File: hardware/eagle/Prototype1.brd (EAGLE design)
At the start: 100 x 80 mm, 27 parts, among them U1 ARDUINO_SHIELDLABEL

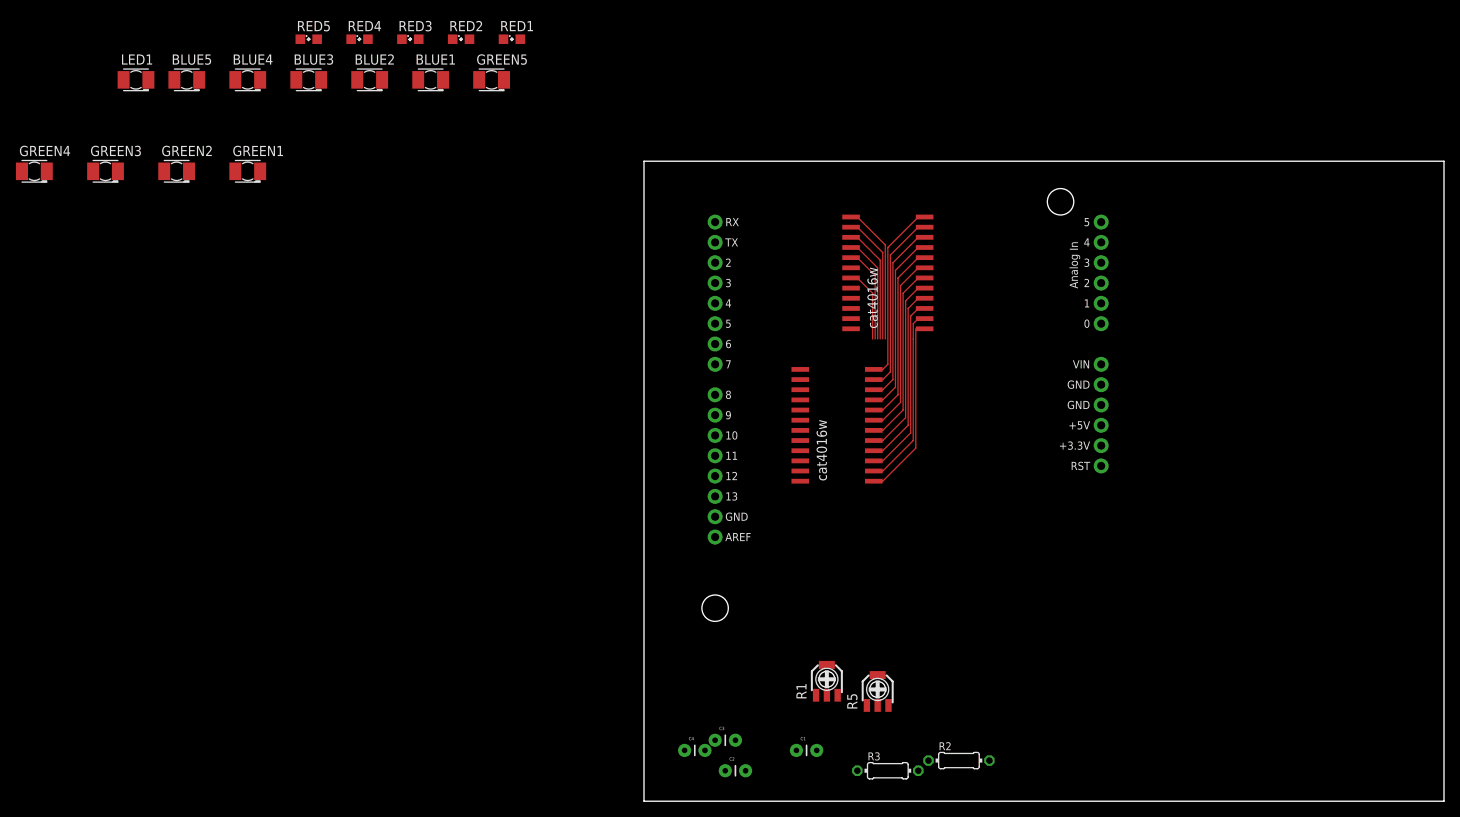
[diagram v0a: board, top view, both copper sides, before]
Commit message: cat4016 hat nun kleine Füsse
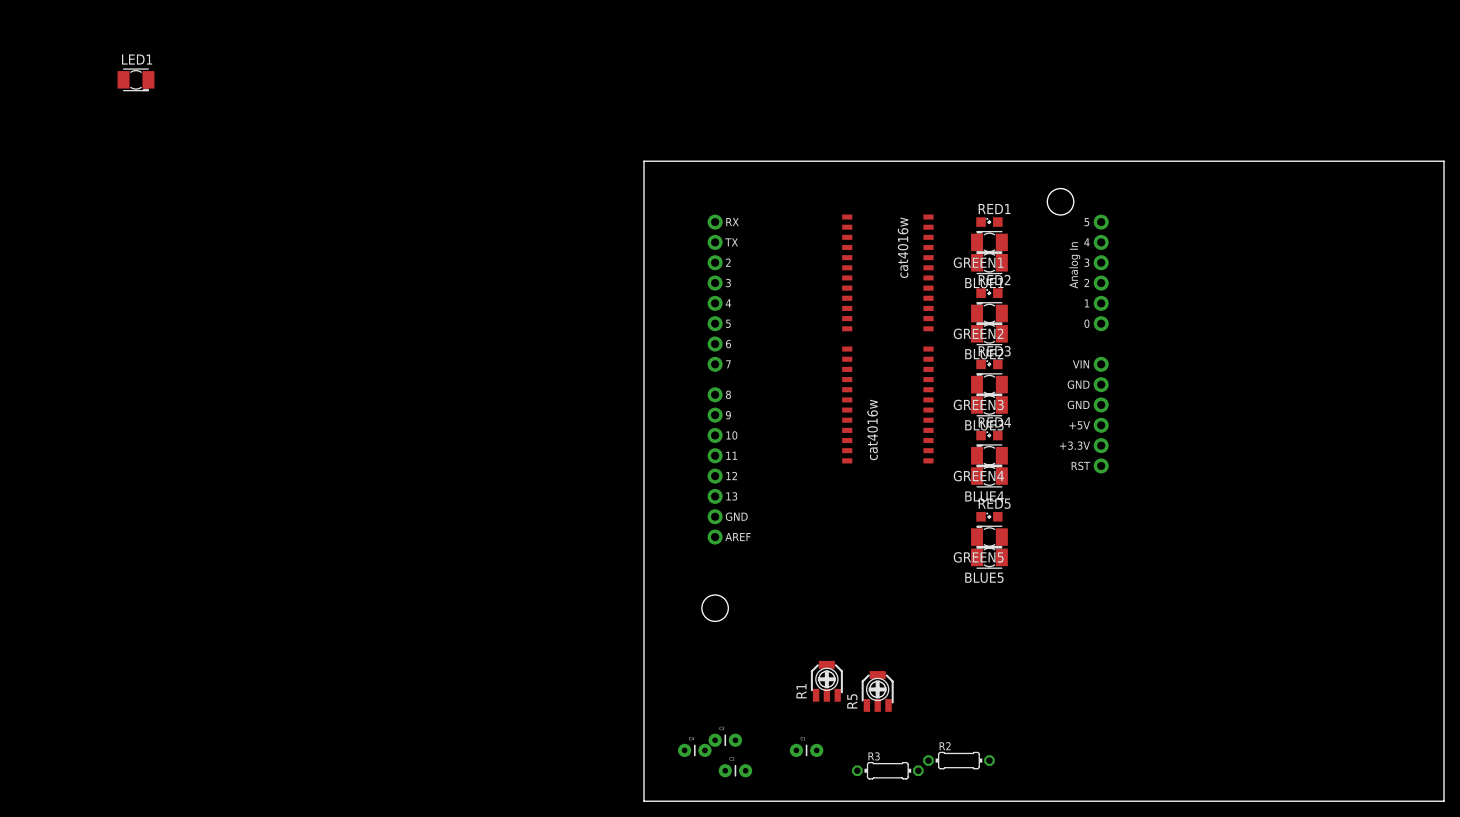
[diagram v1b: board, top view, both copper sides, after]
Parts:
- moved GREEN4 124.6 mm to (43.2, 43.2), turned to 180 degrees
- moved BLUE5 116.7 mm to (43.2, 30.5), turned to 180 degrees
- moved GREEN3 113.7 mm to (43.2, 52.1), turned to 180 degrees
- moved BLUE4 105.1 mm to (43.2, 40.6), turned to 180 degrees
- moved RED5 103.9 mm to (43.2, 35.6)
- moved GREEN2 103.1 mm to (43.2, 61.0), turned to 180 degrees
- moved BLUE3 94.3 mm to (43.2, 49.5), turned to 180 degrees
- moved GREEN1 93.1 mm to (43.2, 69.8), turned to 180 degrees
- moved RED4 93.0 mm to (43.2, 45.7)
- moved GREEN5 84.5 mm to (43.2, 33.0), turned to 180 degrees
- moved BLUE2 83.7 mm to (43.2, 58.4), turned to 180 degrees
- moved RED3 83.0 mm to (43.2, 54.6)
- moved BLUE1 73.5 mm to (43.2, 67.3), turned to 180 degrees
- moved RED2 73.3 mm to (43.2, 63.5)
- moved RED1 63.9 mm to (43.2, 72.4)
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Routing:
- net N$21: track 22.8 -> 0.00 mm
- net N$8: track 22.8 -> 0.00 mm
- net N$25: track 22.8 -> 0.00 mm
- net N$24: track 22.8 -> 0.00 mm
- net N$7: track 22.8 -> 0.00 mm
- net N$23: track 22.8 -> 0.00 mm
- net N$19: track 22.8 -> 0.00 mm
- net N$22: track 22.8 -> 0.00 mm
- net N$20: track 22.8 -> 0.00 mm
- net N$18: track 22.0 -> 0.00 mm
- net GND: track 21.9 -> 0.00 mm
- net N$9: track 19.2 -> 0.00 mm
- net N$17: track 17.5 -> 0.00 mm
- net N$15: track 16.1 -> 0.00 mm
- net N$16: track 14.7 -> 0.00 mm
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
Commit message: Wege bahnen WIP
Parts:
- removed LED1: (no value), led:KA-3528ASYC
- moved C2 64.1 mm to (31.8, 64.1)
- moved C1 61.0 mm to (31.8, 66.0)
- moved C4 26.2 mm to (21.6, 26.7)
- moved C3 24.5 mm to (21.6, 28.6)
- moved R2 23.7 mm to (33.0, 27.9), turned to 180 degrees
- moved R1 14.6 mm to (8.26, 15.2)
- moved R3 13.3 mm to (17.8, 7.62)
- moved U$2 12.1 mm to (29.2, 54.0)
- moved U$3 12.1 mm to (29.2, 37.5)
- moved R5 11.0 mm to (31.1, 24.8), turned to 270 degrees
- moved RED1 4.62 mm to (44.5, 67.9)
- moved GREEN5 4.62 mm to (44.5, 28.6)
- moved RED5 4.62 mm to (44.5, 31.1)
- moved BLUE1 4.62 mm to (44.5, 62.9)
- moved BLUE2 4.62 mm to (44.5, 54.0)
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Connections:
- net N$11: now also RED5.C, U$2.6; no longer BLUE5.C, U$2.19
- net N$12: now also U$2.7; no longer U$2.18
- net N$13: now also BLUE5.C, U$2.8; no longer RED5.C, U$2.17
- net N$14: now also U$2.9; no longer U$2.16
- net N$15: now also U$2.11; no longer U$2.14
- net N$16: now also U$2.10; no longer U$2.15
- net N$17: now also U$2.12; no longer U$2.13
- net N$18: now also U$2.13; no longer U$2.12
- net N$19: now also U$2.14; no longer U$2.11
- net N$20: now also U$2.15; no longer U$2.10
- net N$21: now also U$2.16; no longer U$2.9
- net N$22: now also U$2.17; no longer U$2.8
- net N$23: now also U$2.18; no longer U$2.7
- net N$24: now also U$2.19; no longer U$2.6
- net N$25: now also U$2.20; no longer U$2.5
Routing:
- net +5V: track 0.00 -> 163.7 mm
- net N$25: track 0.00 -> 42.4 mm
- net N$24: track 0.00 -> 37.5 mm
- net N$23: track 0.00 -> 32.6 mm
- net N$8: track 0.00 -> 24.7 mm
- net N$11: track 0.00 -> 22.2 mm
- net N$12: track 0.00 -> 19.1 mm
- net N$22: track 0.00 -> 15.4 mm
- net N$13: track 0.00 -> 15.4 mm
- net N$7: track 0.00 -> 12.9 mm
- net N$14: track 0.00 -> 12.4 mm
- net N$21: track 0.00 -> 12.4 mm
- net N$16: track 0.00 -> 9.94 mm
- net N$26: track 0.00 -> 9.57 mm
- net N$20: track 0.00 -> 9.31 mm
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
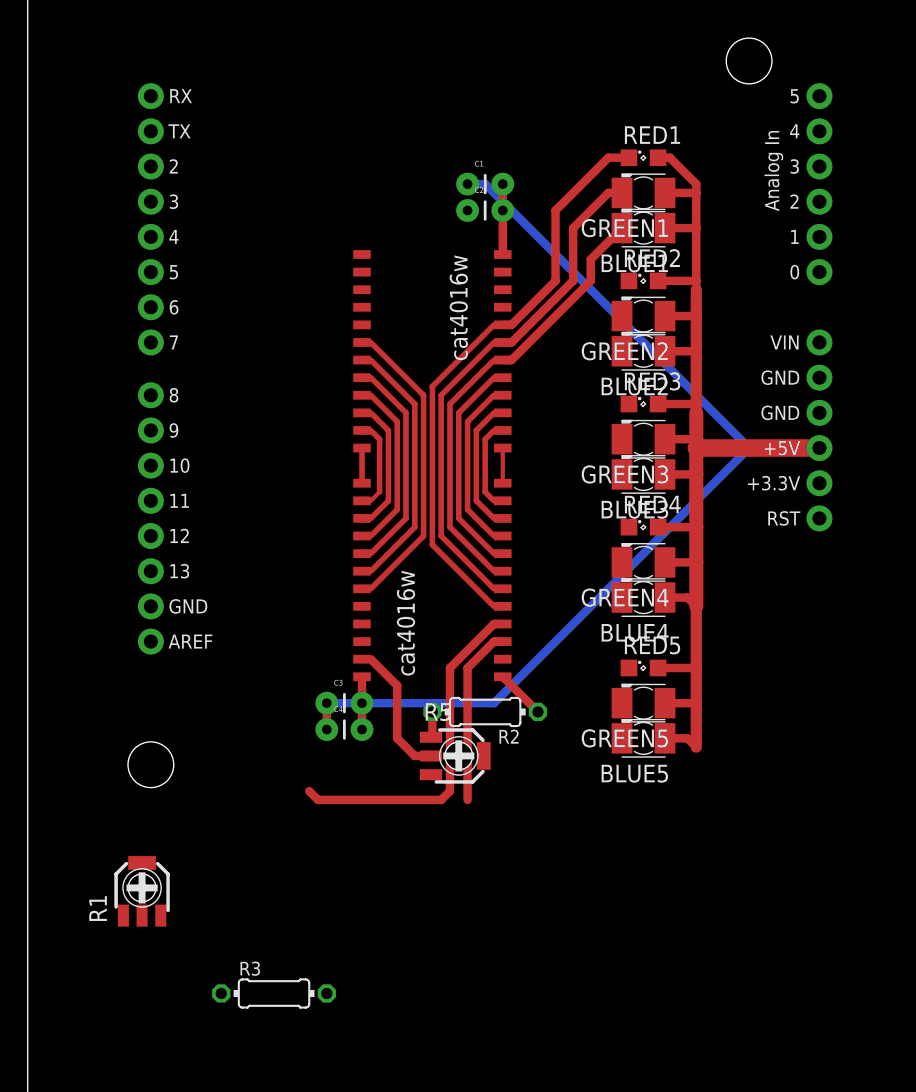
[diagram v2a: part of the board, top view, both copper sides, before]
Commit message: Prototyp 1 verkabelt
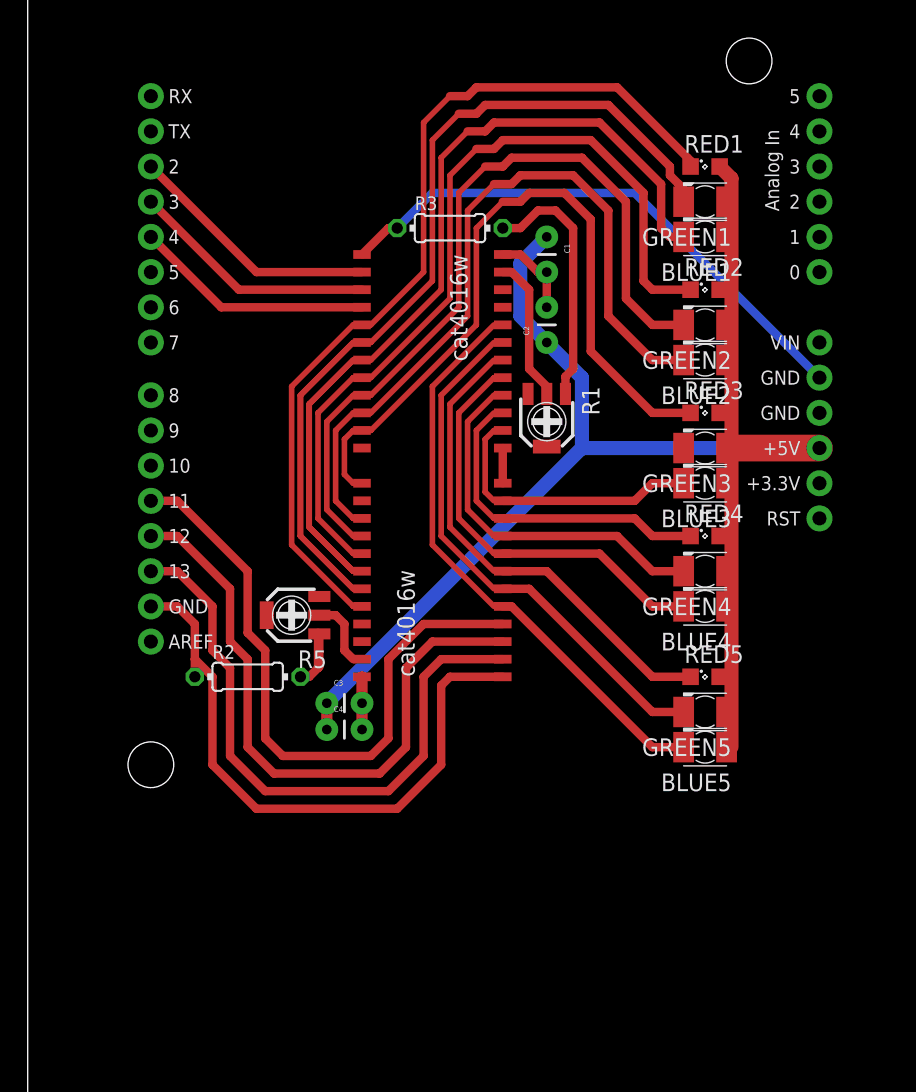
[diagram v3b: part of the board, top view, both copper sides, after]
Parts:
- moved R3 56.7 mm to (30.5, 62.9)
- moved R1 44.6 mm to (37.5, 48.9), turned to 180 degrees
- moved R2 17.3 mm to (15.9, 30.5), turned to 0 degrees
- moved R5 15.8 mm to (19.1, 34.9), turned to 90 degrees
- moved C2 11.1 mm to (37.5, 54.6), turned to 90 degrees
- moved C1 6.87 mm to (37.5, 62.2), turned to 270 degrees
- moved BLUE1 4.49 mm to (48.9, 62.2)
- moved BLUE5 4.49 mm to (48.9, 25.4)
- moved GREEN1 4.49 mm to (48.9, 64.8)
- moved BLUE2 4.49 mm to (48.9, 53.3)
- moved BLUE3 4.49 mm to (48.9, 44.5)
- moved BLUE4 4.49 mm to (48.9, 35.6)
- moved GREEN2 4.49 mm to (48.9, 55.9)
- moved GREEN3 4.49 mm to (48.9, 47.0)
- moved GREEN4 4.49 mm to (48.9, 38.1)
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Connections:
- new net N$31: U$3.4, U1.D11
- new net N$39: BLUE5.C, U$2.20, U$3.5
- net GND: now also U1.GND@1, U1.GND@2
- net N$10: now also U1.D2; no longer U1.D5
- net N$11: now also GREEN2.C, U$2.9, U$3.16; no longer RED5.C, U$2.6, U$3.19
- net N$12: now also RED2.C, U$2.8, U$3.17; no longer GREEN5.C, U$2.7, U$3.18
- net N$13: now also BLUE1.C, U$2.7, U$3.18; no longer BLUE5.C, U$2.8, U$3.17
- net N$14: now also GREEN1.C, U$2.6, U$3.19; no longer BLUE4.C, U$2.9, U$3.16
- net N$15: now also BLUE2.C, U$2.10, U$3.15; no longer RED4.C, U$2.11, U$3.14
- net N$16: now also RED1.C, U$2.5, U$3.20; no longer GREEN4.C, U$2.10, U$3.15
- net N$17: now also RED3.C, U$2.11; no longer BLUE3.C, U$2.12
- net N$19: now also BLUE3.C; no longer RED3.C
- net N$20: now also RED4.C; no longer BLUE2.C
- net N$21: now also GREEN4.C; no longer GREEN2.C
- net N$22: now also BLUE4.C; no longer RED2.C
- net N$23: now also RED5.C; no longer BLUE1.C
- net N$24: now also GREEN5.C; no longer GREEN1.C
- net N$25: now also U$3.3, U1.D12; no longer RED1.C, U$2.20, U$3.5
- net N$7: now also U1.D3; no longer U$3.3, U1.D2
- net N$8: now also U1.D4; no longer U$3.4, U1.D3
- net N$9: now also U1.D13; no longer U1.D4
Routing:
- net GND: track 3.59 -> 85.6 mm
- net N$16: track 9.94 -> 65.7 mm
- net +5V: track 163.7 -> 112.2 mm
- net N$14: track 12.4 -> 63.5 mm
- net N$17: track 2.54 -> 52.7 mm
- net N$15: track 6.24 -> 54.7 mm
- net N$31: track 0.00 -> 46.6 mm
- net N$13: track 15.4 -> 60.3 mm
- net N$9: track 0.00 -> 44.8 mm
- net N$39: track 0.00 -> 41.9 mm
- net N$12: track 19.1 -> 60.3 mm
- net N$11: track 22.2 -> 57.2 mm
- net N$30: track 0.00 -> 20.9 mm
- net N$2: track 0.00 -> 19.0 mm
- net N$10: track 0.00 -> 18.4 mm
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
